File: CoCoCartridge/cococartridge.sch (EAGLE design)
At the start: 52 parts, among them IC1 LPC1769, IC2 LD1117S33, IC3 DP83848C, P1 COCO-CART3.5X2.5, Q1 BSS84

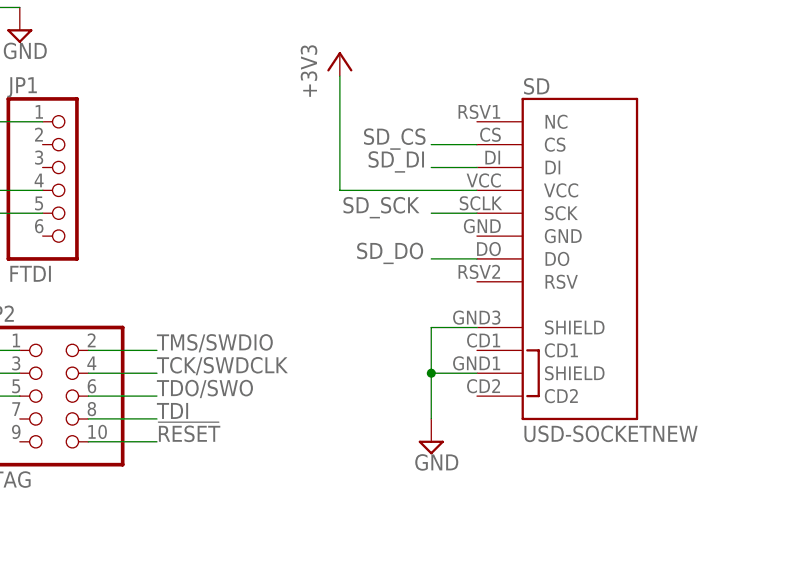
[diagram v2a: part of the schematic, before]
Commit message: Fix missing Gnd connection on SD socket
I connected the shield pins labelled ground to the actual ground but
forgot to connect the actual ground pin of the SD card to my ground
plane.
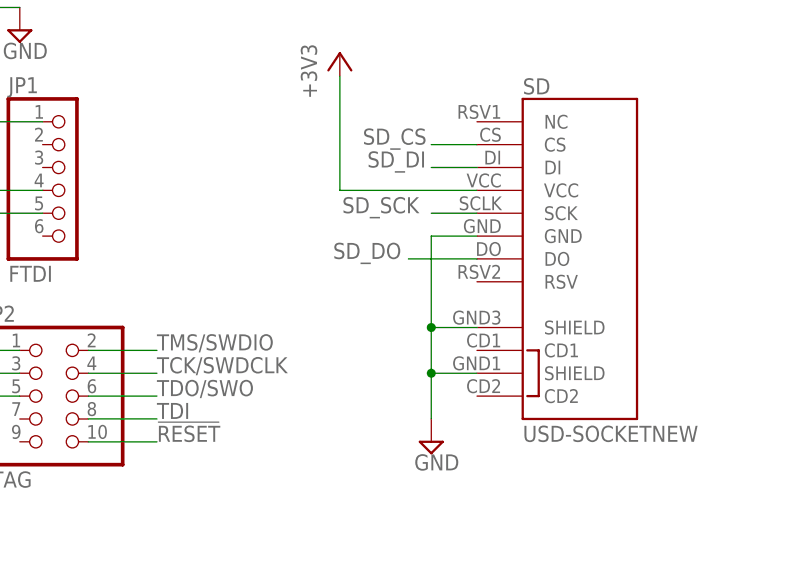
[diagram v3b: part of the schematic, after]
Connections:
- net GND: now also SD.GND
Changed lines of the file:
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@@
 <wire x1="444.5" y1="50.8" x2="444.5" y2="45.72" width="0.1524" layer="91"/>
 <junction x="444.5" y="45.72"/>
+<pinref part="SD" gate="G$1" pin="GND"/>
+<wire x1="449.58" y1="60.96" x2="444.5" y2="60.96" width="0.1524" layer="91"/>
+<wire x1="444.5" y1="60.96" x2="444.5" y2="50.8" width="0.1524" layer="91"/>
+<junction x="444.5" y="50.8"/>
 </segment>
 <segment>
@@
 <segment>
 <pinref part="SD" gate="G$1" pin="DO"/>
-<wire x1="449.58" y1="58.42" x2="444.5" y2="58.42" width="0.1524" layer="91"/>
-<label x="436.118" y="58.42" size="1.778" layer="95"/>
-</segment>
-</net>
+<wire x1="449.58" y1="58.42" x2="441.96" y2="58.42" width="0.1524" layer="91"/>
+<label x="433.578" y="58.42" size="1.778" layer="95"/>
+</segment>
+</net>
